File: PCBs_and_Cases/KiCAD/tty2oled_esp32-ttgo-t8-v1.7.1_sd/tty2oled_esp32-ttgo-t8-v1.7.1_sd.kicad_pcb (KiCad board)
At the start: 2 copper layers, 35.6 x 99.7 mm, 2 parts

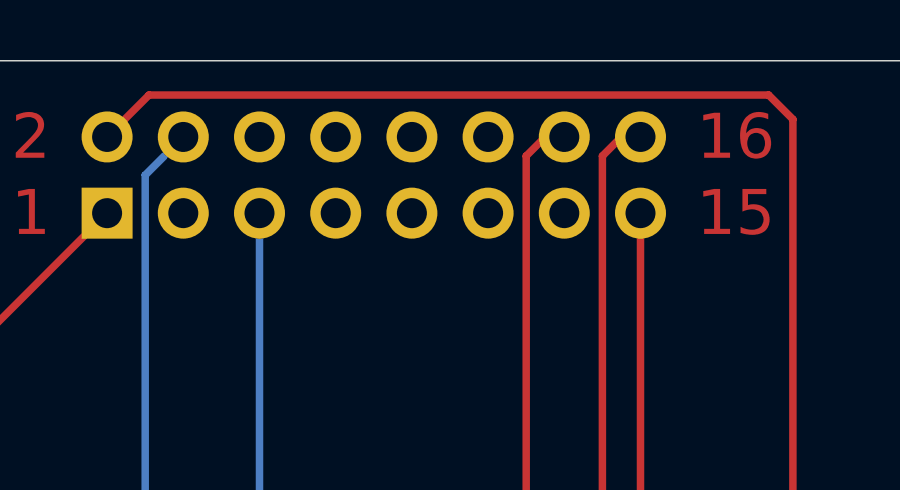
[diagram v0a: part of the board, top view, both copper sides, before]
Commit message: KiCAD: GNDs added, files renamed
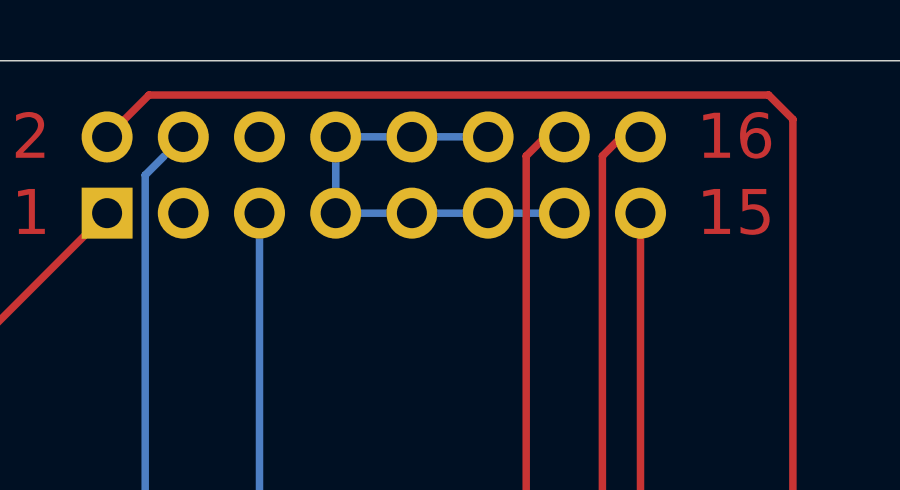
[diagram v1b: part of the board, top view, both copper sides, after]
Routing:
- net (no net): track 503.3 -> 518.6 mm

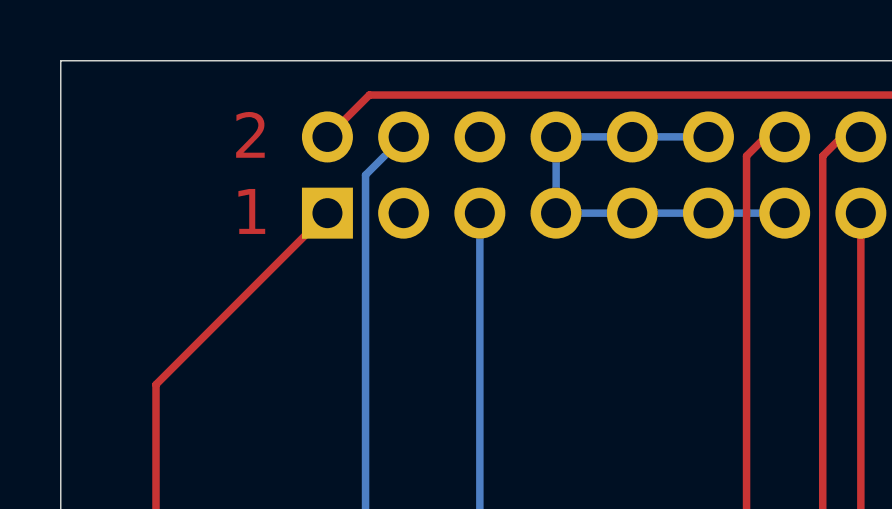
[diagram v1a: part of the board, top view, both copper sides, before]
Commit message: GND was missing in KiCAD/Gerbers
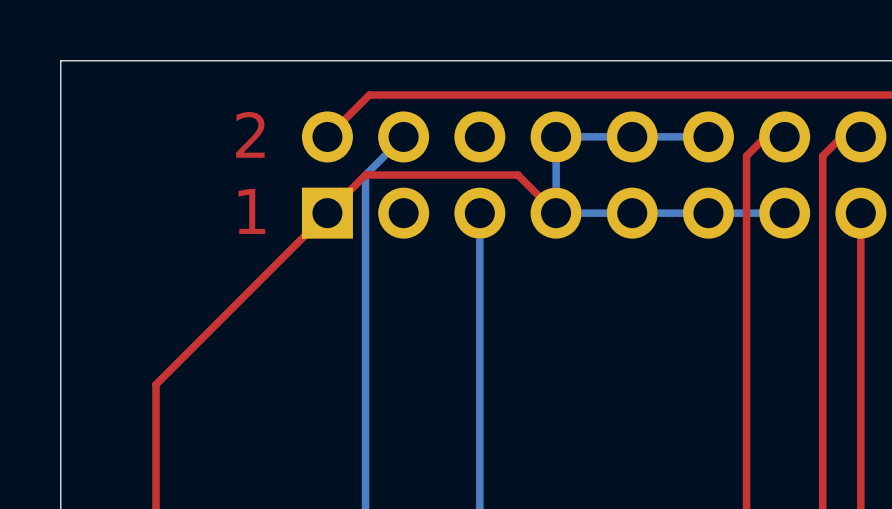
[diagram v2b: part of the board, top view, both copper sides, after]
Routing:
- net (no net): track 518.6 -> 527.3 mm

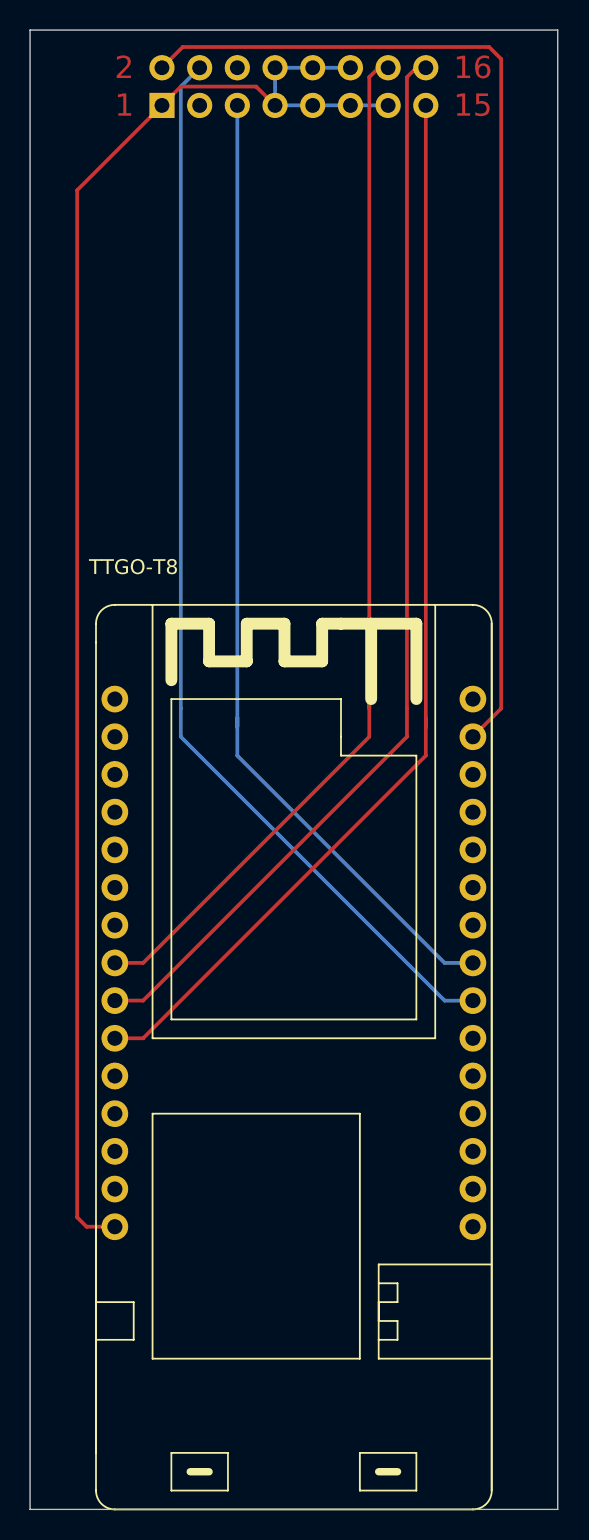
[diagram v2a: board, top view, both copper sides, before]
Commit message: ESP32-DevKitC removed, Lolin32 added
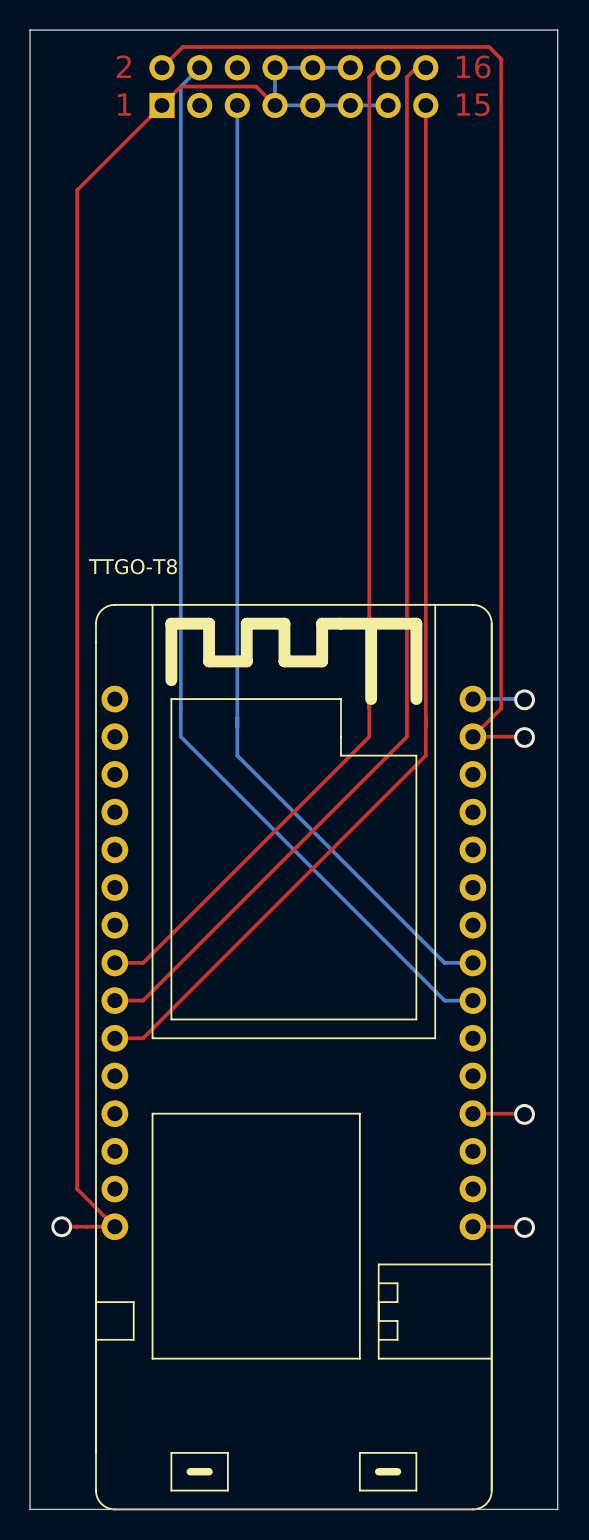
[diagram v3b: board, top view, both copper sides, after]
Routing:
- net (no net): track 527.3 -> 543.8 mm, vias 0 -> 5
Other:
- board text added: "3V"
- board text added: "5V"
- board text added: "GND"
- board text added: "MiSTer_tty2oled Idea: Venice Desgin: RealLarry"
- board text added: "Thanks to Sorgelig, Jukk@M, Jotego, tf_hh and all other developers"
- board text added: "v1.0"
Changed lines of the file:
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@@
-(kicad_pcb (version 20171130) (host pcbnew 5.1.9)
+(kicad_pcb (version 20171130) (host pcbnew 5.1.10)
   (general
     (thickness 1.6)
-    (drawings 11)
-    (tracks 40)
+    (drawings 19)
+    (tracks 57)
     (zones 0)
     (modules 2)
@@
     )
   )
+  (gr_text GND (at 134.1628 133.6548) (layer F.Paste)
+    (effects (font (size 1 1) (thickness 0.15)))
+  )
+  (gr_text 5V (at 165.4048 133.8072) (layer F.Paste)
+    (effects (font (size 1 1) (thickness 0.15)))
+  )
+  (gr_text GND (at 165.354 126.1872) (layer F.Paste)
+    (effects (font (size 1 1) (thickness 0.15)))
+  )
+  (gr_text 3V (at 165.354 100.7872) (layer F.Paste)
+    (effects (font (size 1 1) (thickness 0.15)))
+  )
+  (gr_text GND (at 165.4556 95.0468) (layer F.Paste)
+    (effects (font (size 1 1) (thickness 0.15)))
+  )
+  (gr_text v1.0 (at 137.9855 73.1774 -90) (layer F.Paste)
+    (effects (font (size 1 1) (thickness 0.15)))
+  )
+  (gr_text "MiSTer_tty2oled\nIdea: Venice\nDesgin: RealLarry" (at 149.4917 73.9648 -90) (layer F.Paste)
+    (effects (font (size 1 1) (thickness 0.15)))
+  )
+  (gr_text "Thanks to Sorgelig,\nJukk@M, Jotego, tf_hh\nand all other developers" (at 142.5956 73.7616 -90) (layer F.Paste)
+    (effects (font (size 1 1) (thickness 0.15)))
+  )
   (dimension 60.96 (width 0.15) (layer Dwgs.User)
     (gr_text "60,960 mm" (at 118.715 120.65 90) (layer Dwgs.User)
@@
   (segment (start 154.94 97.155) (end 154.94 96.52) (width 0.25) (layer F.Cu) (net 0))
   (segment (start 137.795 132.08) (end 135.89 132.08) (width 0.25) (layer F.Cu) (net 0))
-  (segment (start 135.89 132.08) (end 135.255 131.445) (width 0.25) (layer F.Cu) (net 0))
-  (segment (start 135.255 62.23) (end 140.97 56.515) (width 0.25) (layer F.Cu) (net 0))
-  (segment (start 135.255 131.445) (end 135.255 62.23) (width 0.25) (layer F.Cu) (net 0))
   (segment (start 140.97 53.975) (end 142.367 52.578) (width 0.25) (layer F.Cu) (net 0))
   (segment (start 163.021194 52.578) (end 163.83 53.386806) (width 0.25) (layer F.Cu) (net 0))
@@
   (segment (start 148.59 56.515) (end 147.32 55.245) (width 0.25) (layer F.Cu) (net 0))
   (segment (start 147.32 55.245) (end 142.24 55.245) (width 0.25) (layer F.Cu) (net 0))
+  (via (at 134.2136 132.08) (size 1.4) (drill 1) (layers F.Cu B.Cu) (net 0))
+  (segment (start 135.255 132.0546) (end 135.2296 132.08) (width 0.25) (layer F.Cu) (net 0))
+  (segment (start 140.97 56.515) (end 135.255 62.23) (width 0.25) (layer F.Cu) (net 0))
+  (segment (start 135.2296 132.08) (end 135.89 132.08) (width 0.25) (layer F.Cu) (net 0))
+  (segment (start 134.2136 132.08) (end 135.2296 132.08) (width 0.25) (layer F.Cu) (net 0))
+  (via (at 165.4048 132.1308) (size 1.4) (drill 1) (layers F.Cu B.Cu) (net 0))
+  (via (at 165.4048 124.5108) (size 1.4) (drill 1) (layers F.Cu B.Cu) (net 0))
+  (via (at 165.4048 99.1108) (size 1.4) (drill 1) (layers F.Cu B.Cu) (net 0))
+  (via (at 165.4048 96.5708) (size 1.4) (drill 1) (layers F.Cu B.Cu) (net 0))
+  (segment (start 165.354 132.08) (end 165.4048 132.1308) (width 0.25) (layer F.Cu) (net 0))
+  (segment (start 161.925 132.08) (end 165.354 132.08) (width 0.25) (layer F.Cu) (net 0))
+  (segment (start 165.354 124.46) (end 165.4048 124.5108) (width 0.25) (layer F.Cu) (net 0))
+  (segment (start 161.925 124.46) (end 165.354 124.46) (width 0.25) (layer F.Cu) (net 0))
+  (segment (start 165.354 99.06) (end 165.4048 99.1108) (width 0.25) (layer F.Cu) (net 0))
+  (segment (start 161.925 99.06) (end 165.354 99.06) (width 0.25) (layer F.Cu) (net 0))
+  (segment (start 165.354 96.52) (end 165.4048 96.5708) (width 0.25) (layer B.Cu) (net 0))
+  (segment (start 161.925 96.52) (end 165.354 96.52) (width 0.25) (layer B.Cu) (net 0))
+  (segment (start 135.255 129.54) (end 135.255 129.413) (width 0.25) (layer F.Cu) (net 0))
+  (segment (start 137.795 132.08) (end 135.255 129.54) (width 0.25) (layer F.Cu) (net 0))
+  (segment (start 135.255 62.23) (end 135.255 129.413) (width 0.25) (layer F.Cu) (net 0))
 )

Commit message: Silkscreen fixed
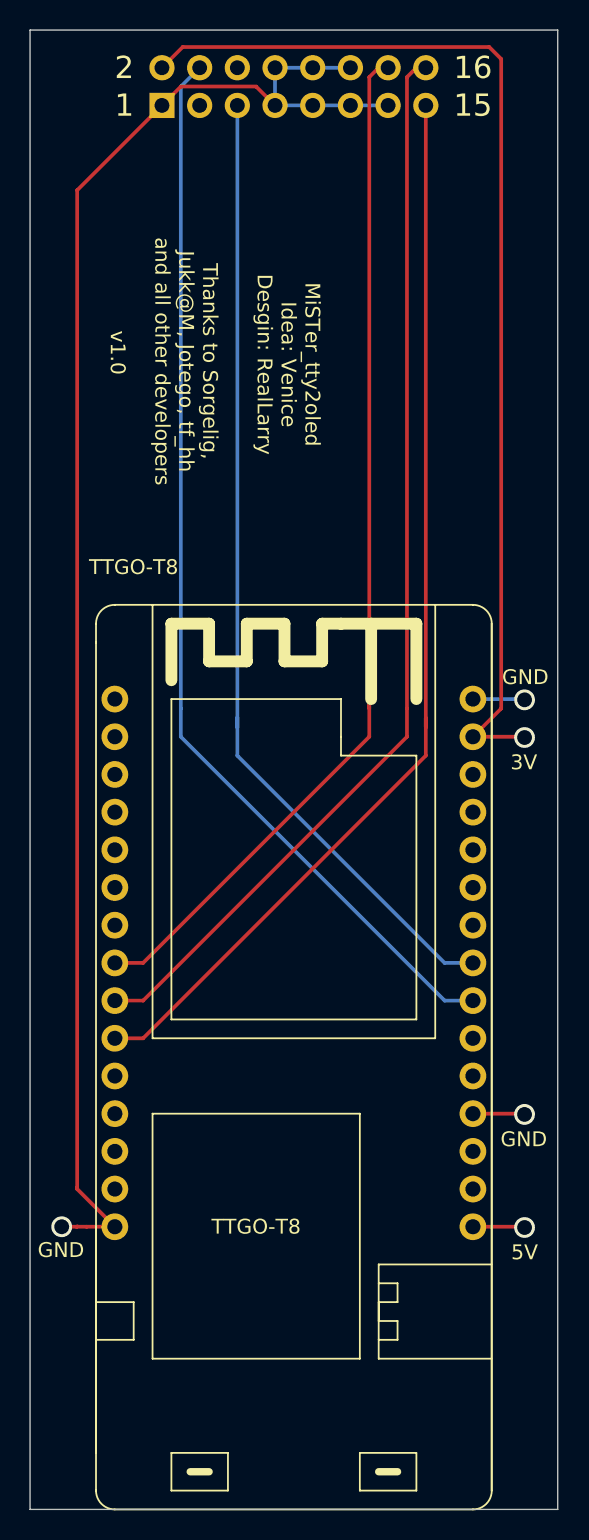
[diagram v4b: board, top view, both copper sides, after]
